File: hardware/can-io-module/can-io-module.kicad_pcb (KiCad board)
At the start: 2 copper layers, 96 x 86 mm, 12 parts, among them J1 ECU_FCI_24P_RightAngle, Q4 RELAY1 MOSFET, Q5 RELAY2 MOSFET, U1 STM32G0B1CBT6, U10 MAX31855K, U11 FLEX SCHMITT, U2 LMR16006Y-Q1, U5 74HCT4051-1K, U6 74HCT4051-4K7, U7 L9613, U8 TJA1051T/3, U9 TLV9002-Q1

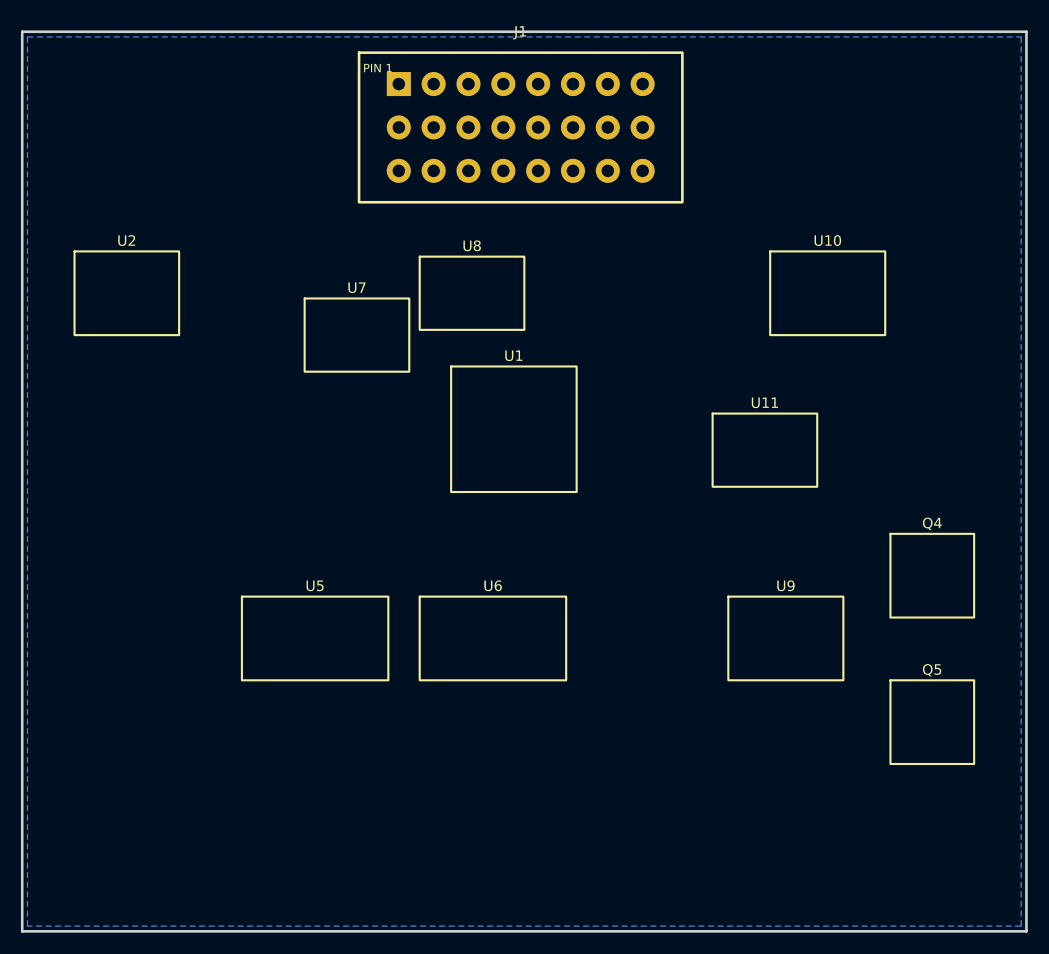
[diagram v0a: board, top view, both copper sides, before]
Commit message: feat: generate connected CAN IO revision B PCB
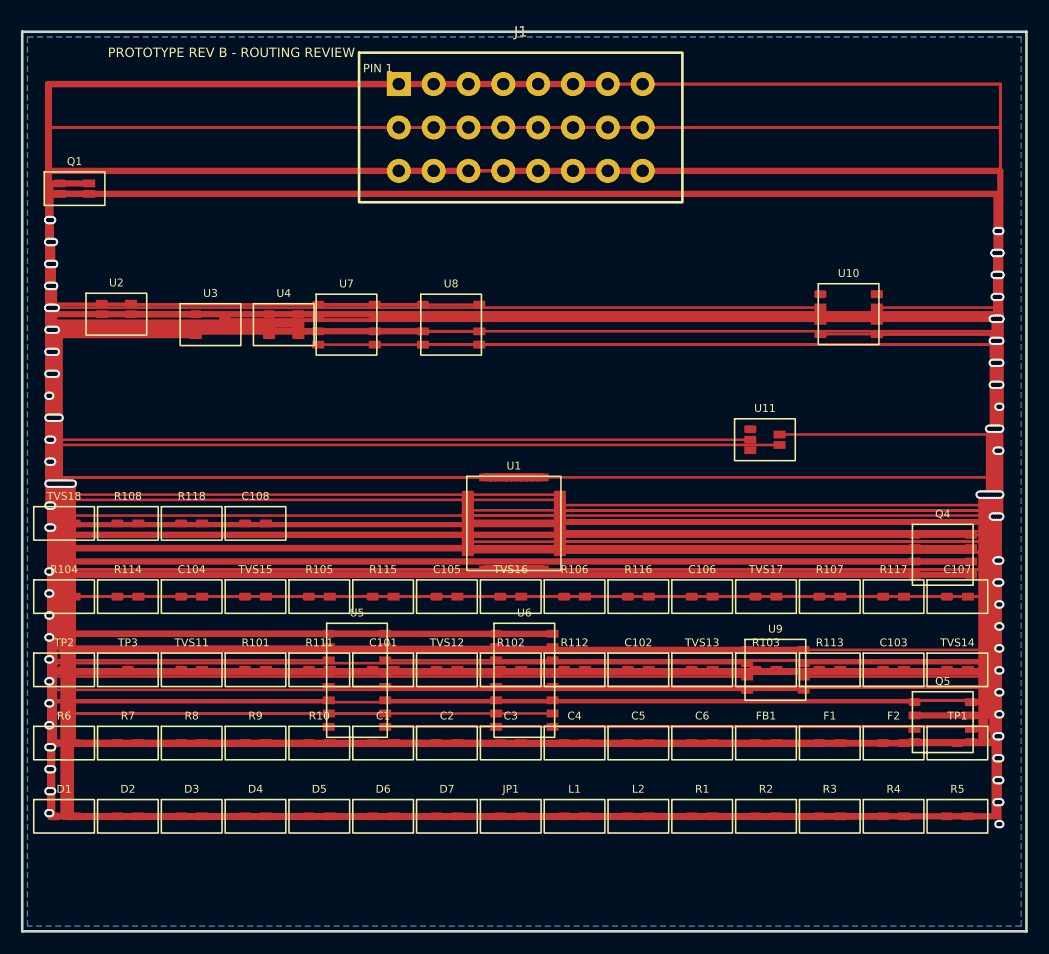
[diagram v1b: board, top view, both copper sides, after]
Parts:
- added C1: 10uF 50V input, DIY_DASH:1210, F.Cu at (54.5, 88.0)
- added C101: 100nF ADC filter, DIY_DASH:0603, F.Cu at (54.5, 81.0)
- added C102: 100nF ADC filter, DIY_DASH:0603, F.Cu at (78.9, 81.0)
- added C103: 100nF ADC filter, DIY_DASH:0603, F.Cu at (103.3, 81.0)
- added C104: 100nF ADC filter, DIY_DASH:0603, F.Cu at (36.2, 74.0)
- added C105: 100nF ADC filter, DIY_DASH:0603, F.Cu at (60.6, 74.0)
- added C106: 100nF ADC filter, DIY_DASH:0603, F.Cu at (85.0, 74.0)
- added C107: 100nF ADC filter, DIY_DASH:0603, F.Cu at (109.4, 74.0)
- added C108: 100nF ADC filter, DIY_DASH:0603, F.Cu at (42.3, 67.0)
- added C2: 22uF 10V buck output, DIY_DASH:1206, F.Cu at (60.6, 88.0)
- added C3: 4.7uF 10V 3V3 bulk, DIY_DASH:0805, F.Cu at (66.7, 88.0)
- added C4: 100nF U1 VDD1, DIY_DASH:0603, F.Cu at (72.8, 88.0)
- added C5: 100nF U1 VDD2, DIY_DASH:0603, F.Cu at (78.9, 88.0)
- added C6: 100nF U1 VDDA, DIY_DASH:0603, F.Cu at (85.0, 88.0)
- added D1: SMBJ33A, DIY_DASH:SMB_DO-214AA, F.Cu at (24.0, 95.0)
- added D2: Buck catch diode 60V, DIY_DASH:SMA_DO-214AC, F.Cu at (30.1, 95.0)
- added D3: CAN TVS, DIY_DASH:SOT23, F.Cu at (36.2, 95.0)
- added D4: K-line TVS 24V, DIY_DASH:SMA_DO-214AC, F.Cu at (42.3, 95.0)
- added D5: Flex TVS 5V, DIY_DASH:SOD323, F.Cu at (48.4, 95.0)
- added D6: AOUT1 ESD, DIY_DASH:SOD323, F.Cu at (54.5, 95.0)
- added D7: AOUT2 ESD, DIY_DASH:SOD323, F.Cu at (60.6, 95.0)
- added F1: 1A input fuse, DIY_DASH:NANO2_2410, F.Cu at (97.2, 88.0)
- added F2: 250mA resettable sensor fuse, DIY_DASH:1206, F.Cu at (103.3, 88.0)
- added FB1: 600R ferrite VDDA, DIY_DASH:0603, F.Cu at (91.1, 88.0)
- added JP1: 120R CAN termination, DIY_DASH:0603, F.Cu at (66.7, 95.0)
- added L1: 22uH buck inductor, DIY_DASH:5.5x5.5mm, F.Cu at (72.8, 95.0)
- added L2: CAN common-mode choke, DIY_DASH:1812_common-mode, F.Cu at (78.9, 95.0)
- added Q1: 60V P-channel reverse polarity, DIY_DASH:PowerPAK_SO-8, F.Cu at (25.0, 35.0)
- added R1: 1.00k 1% excitation, DIY_DASH:0603, F.Cu at (85.0, 95.0)
- added R10: 100k BOOT0 pull-down, DIY_DASH:0603, F.Cu at (48.4, 88.0)
- added R101: 10.0k 1% AIN series, DIY_DASH:0603, F.Cu at (42.3, 81.0)
- added R102: 10.0k 1% AIN series, DIY_DASH:0603, F.Cu at (66.7, 81.0)
- added R103: 10.0k 1% AIN series, DIY_DASH:0603, F.Cu at (91.1, 81.0)
- added R104: 10.0k 1% AIN series, DIY_DASH:0603, F.Cu at (24.0, 74.0)
- added R105: 10.0k 1% AIN series, DIY_DASH:0603, F.Cu at (48.4, 74.0)
- added R106: 10.0k 1% AIN series, DIY_DASH:0603, F.Cu at (72.8, 74.0)
- added R107: 10.0k 1% AIN series, DIY_DASH:0603, F.Cu at (97.2, 74.0)
- added R108: 10.0k 1% AIN series, DIY_DASH:0603, F.Cu at (30.1, 67.0)
- added R111: 15.0k 1% AIN lower, DIY_DASH:0603, F.Cu at (48.4, 81.0)
- added R112: 15.0k 1% AIN lower, DIY_DASH:0603, F.Cu at (72.8, 81.0)
- added R113: 15.0k 1% AIN lower, DIY_DASH:0603, F.Cu at (97.2, 81.0)
- added R114: 15.0k 1% AIN lower, DIY_DASH:0603, F.Cu at (30.1, 74.0)
- added R115: 15.0k 1% AIN lower, DIY_DASH:0603, F.Cu at (54.5, 74.0)
- added R116: 15.0k 1% AIN lower, DIY_DASH:0603, F.Cu at (78.9, 74.0)
- added R117: 15.0k 1% AIN lower, DIY_DASH:0603, F.Cu at (103.3, 74.0)
- added R118: 15.0k 1% AIN lower, DIY_DASH:0603, F.Cu at (36.2, 67.0)
- added R2: 4.70k 1% excitation, DIY_DASH:0603, F.Cu at (91.1, 95.0)
- added R3: 100k mux enable safe-state, DIY_DASH:0603, F.Cu at (97.2, 95.0)
- added R4: 100k mux enable safe-state, DIY_DASH:0603, F.Cu at (103.3, 95.0)
- added R5: 100k relay gate pull-down, DIY_DASH:0603, F.Cu at (109.4, 95.0)
- added R6: 100k relay gate pull-down, DIY_DASH:0603, F.Cu at (24.0, 88.0)
- added R7: 220R AOUT1 isolation, DIY_DASH:0603, F.Cu at (30.1, 88.0)
- added R8: 220R AOUT2 isolation, DIY_DASH:0603, F.Cu at (36.2, 88.0)
- added R9: 10k NRST pull-up, DIY_DASH:0603, F.Cu at (42.3, 88.0)
- added TP1: SWDIO, DIY_DASH:Test_pad, F.Cu at (109.4, 88.0)
- added TP2: SWCLK, DIY_DASH:Test_pad, F.Cu at (24.0, 81.0)
- added TP3: NRST, DIY_DASH:Test_pad, F.Cu at (30.1, 81.0)
- added TVS11: AIN1 low-leakage ESD, DIY_DASH:SOD323, F.Cu at (36.2, 81.0)
- added TVS12: AIN2 low-leakage ESD, DIY_DASH:SOD323, F.Cu at (60.6, 81.0)
- added TVS13: AIN3 low-leakage ESD, DIY_DASH:SOD323, F.Cu at (85.0, 81.0)
- added TVS14: AIN4 low-leakage ESD, DIY_DASH:SOD323, F.Cu at (109.4, 81.0)
- added TVS15: AIN5 low-leakage ESD, DIY_DASH:SOD323, F.Cu at (42.3, 74.0)
- added TVS16: AIN6 low-leakage ESD, DIY_DASH:SOD323, F.Cu at (66.7, 74.0)
- added TVS17: AIN7 low-leakage ESD, DIY_DASH:SOD323, F.Cu at (91.1, 74.0)
- added TVS18: AIN8 low-leakage ESD, DIY_DASH:SOD323, F.Cu at (24.0, 67.0)
- added U3: 3V3 LDO 300mA, DIY_DASH:SOT-23-5, F.Cu at (38.0, 48.0)
- added U4: SENSOR_5V load switch, DIY_DASH:SC70-6, F.Cu at (45.0, 48.0)
- Q4: value RELAY1 MOSFET -> 60V logic N-MOS RELAY1; footprint DIY_DASH:PLACEMENT_BLOCK -> DIY_DASH:LFPAK56
- Q5: value RELAY2 MOSFET -> 60V logic N-MOS RELAY2; footprint DIY_DASH:PLACEMENT_BLOCK -> DIY_DASH:LFPAK56
- U1: footprint DIY_DASH:PLACEMENT_BLOCK -> DIY_DASH:LQFP-48_7x7mm
- U10: value MAX31855K -> MAX31855KASA+; footprint DIY_DASH:PLACEMENT_BLOCK -> DIY_DASH:SOIC-8_narrow
- U11: value FLEX SCHMITT -> Schmitt Flex front end; footprint DIY_DASH:PLACEMENT_BLOCK -> DIY_DASH:SOT-353
- U2: footprint DIY_DASH:PLACEMENT_BLOCK -> DIY_DASH:SOT-23-THN-6_DDC
- U5: value 74HCT4051-1K -> 74HCT4051 1K excitation; footprint DIY_DASH:PLACEMENT_BLOCK -> DIY_DASH:SOIC-16
- U6: value 74HCT4051-4K7 -> 74HCT4051 4K7 excitation; footprint DIY_DASH:PLACEMENT_BLOCK -> DIY_DASH:SOIC-16
- U7: footprint DIY_DASH:PLACEMENT_BLOCK -> DIY_DASH:SO-8
- U8: footprint DIY_DASH:PLACEMENT_BLOCK -> DIY_DASH:SO-8_SOT96-1
- U9: footprint DIY_DASH:PLACEMENT_BLOCK -> DIY_DASH:SOIC-8
- moved U1 9.00 mm to (67.0, 67.0)
- moved U5 5.66 mm to (52.0, 82.0)
- moved U6 5.00 mm to (68.0, 82.0)
- moved U8 3.61 mm to (61.0, 48.0)
- moved U9 3.16 mm to (92.0, 81.0)
- moved U10 2.83 mm to (99.0, 47.0)
- moved Q4 2.24 mm to (108.0, 70.0)
- moved U2 2.24 mm to (29.0, 47.0)
- moved U7 1.41 mm to (51.0, 48.0)
- moved Q5 1.00 mm to (108.0, 86.0)
- moved U11 1.00 mm to (91.0, 59.0)
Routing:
- net +5V: track 0.00 -> 937.6 mm, vias 0 -> 14
- net +3V3: track 0.00 -> 746.8 mm, vias 0 -> 12
- net RELAY_OUT1: track 0.00 -> 662.0 mm, vias 0 -> 7
- net VBAT_PROTECTED: track 0.00 -> 502.8 mm, vias 0 -> 5
- net AIN8: track 0.00 -> 427.8 mm, vias 0 -> 5
- net ADC_IN4: track 0.00 -> 420.4 mm, vias 0 -> 4
- net ADC_IN3: track 0.00 -> 410.4 mm, vias 0 -> 4
- net AIN2: track 0.00 -> 408.1 mm, vias 0 -> 5
- net AIN3: track 0.00 -> 394.7 mm, vias 0 -> 5
- net ADC_IN7: track 0.00 -> 393.0 mm, vias 0 -> 4
- net AIN4: track 0.00 -> 387.2 mm, vias 0 -> 5
- net AIN7: track 0.00 -> 382.8 mm, vias 0 -> 5
- net AIN6: track 0.00 -> 371.9 mm, vias 0 -> 5
- net ADC_IN8: track 0.00 -> 362.2 mm, vias 0 -> 4
- net CAN_H: track 0.00 -> 353.5 mm, vias 0 -> 4
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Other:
- board text added: "PROTOTYPE REV B - ROUTING REVIEW"
- board text added: "ZONE_POWER ZONE_MCU_COMMS ZONE_ANALOG ZONE_EGT ZONE_OUTPUTS"
- board text removed: "ANALOG INPUTS"
- board text removed: "EGT - QUIET ZONE"
- board text removed: "MCU / CAN / K-LINE"
- board text removed: "OUTPUTS"
- board text removed: "POWER"
- board text removed: "PROTOTYPE REV A"
- board text removed: "ZONE_ANALOG"
- board text removed: "ZONE_EGT"
- board text removed: "ZONE_MCU_COMMS"
- board text removed: "ZONE_OUTPUTS"
- board text removed: "ZONE_POWER"

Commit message: fix: optimize two-layer CAN IO placement
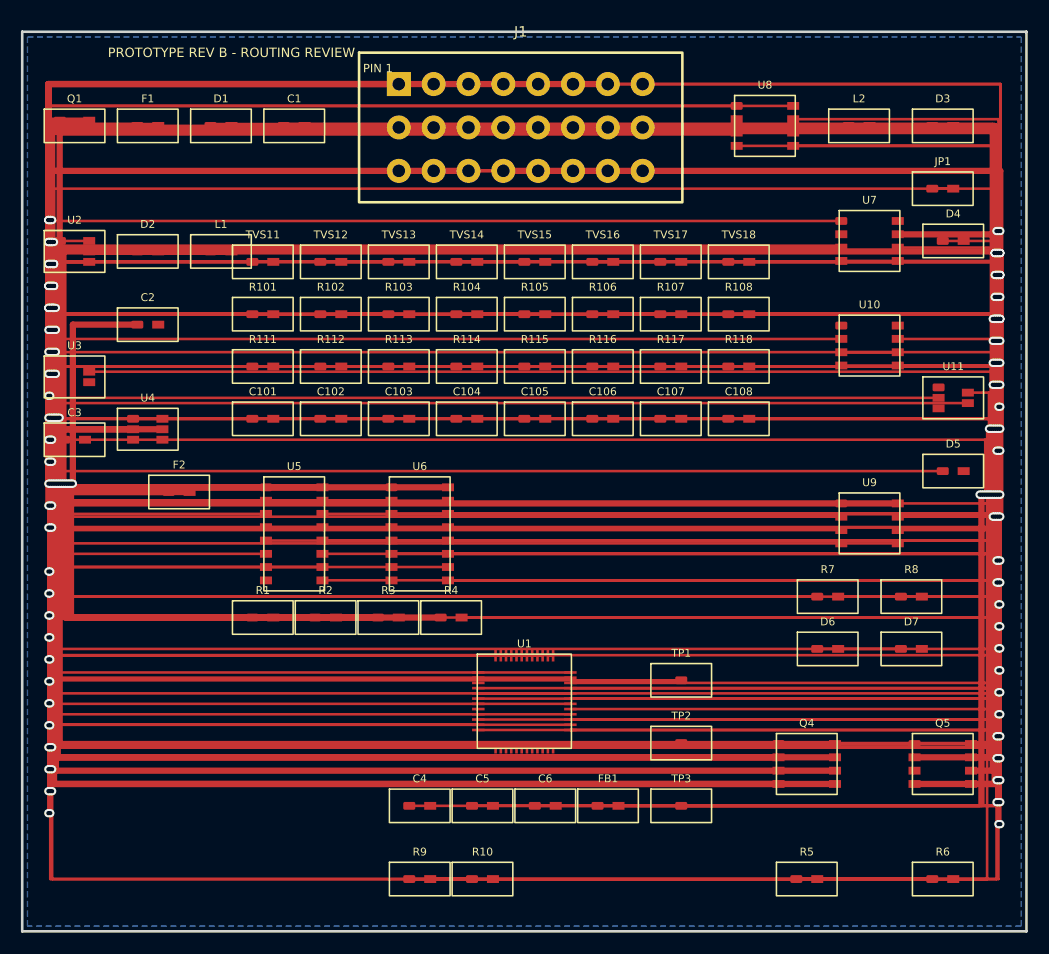
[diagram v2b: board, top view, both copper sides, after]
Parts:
- moved D3 97.5 mm to (108.0, 29.0)
- moved F1 87.9 mm to (32.0, 29.0)
- moved D4 86.5 mm to (109.0, 40.0)
- moved R6 85.0 mm to (108.0, 101.0)
- moved JP1 72.8 mm to (108.0, 35.0)
- moved F2 72.4 mm to (35.0, 64.0)
- moved R8 70.2 mm to (105.0, 74.0)
- moved L2 69.3 mm to (100.0, 29.0)
- moved TVS18 69.2 mm to (88.5, 42.0)
- moved D5 69.0 mm to (109.0, 62.0)
- moved R7 68.3 mm to (97.0, 74.0)
- moved D1 67.7 mm to (39.0, 29.0)
- moved L1 63.7 mm to (39.0, 41.0)
- moved R108 61.7 mm to (88.5, 47.0)
- moved TVS14 61.0 mm to (62.5, 42.0)
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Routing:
- net +5V: track 937.6 -> 610.4 mm
- net CAN_H: track 353.5 -> 127.5 mm
- net ADC_IN3: track 410.4 -> 217.8 mm
- net SENSOR_5V: track 349.4 -> 161.8 mm
- net ADC_IN8: track 362.2 -> 177.3 mm
- net K_LINE: track 248.2 -> 80.3 mm
- net AIN3: track 394.7 -> 229.6 mm
- net ADC_IN4: track 420.4 -> 273.1 mm
- net AIN8: track 427.8 -> 284.9 mm
- net AOUT1: track 272.9 -> 133.5 mm
- net AOUT2_OP: track 248.8 -> 120.0 mm
- net ADC_IN7: track 393.0 -> 281.1 mm
- net VBAT: track 170.2 -> 64.0 mm
- net AIN1: track 301.8 -> 201.1 mm
- net +3V3: track 746.8 -> 843.1 mm
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
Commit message: fix: preserve complete two-layer route
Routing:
- added copper zone on F.Cu, net POWER_GND
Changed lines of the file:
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@@
   (group "ROUTED_POWER_TREE" (id b7391667-93ed-535d-b822-70054c11cea7) (members))
   (group "ROUTED_COMMS_EGT_OUTPUTS" (id ce7aa9ae-598b-5771-b386-408a4e588b00) (members))
+  (zone (net 2) (net_name "POWER_GND") (layer "F.Cu") (hatch edge 0.5) (connect_pads (clearance 0.25)) (min_thickness 0.25) (fill yes (thermal_gap 0.3) (thermal_bridge_width 0.3)) (polygon (pts (xy 20.5 20.5) (xy 115.5 20.5) (xy 115.5 105.5) (xy 20.5 105.5))))
   (zone (net 2) (net_name "POWER_GND") (layer "B.Cu") (hatch edge 0.5) (connect_pads (clearance 0.25)) (min_thickness 0.25) (fill yes (thermal_gap 0.3) (thermal_bridge_width 0.3)) (polygon (pts (xy 20.5 20.5) (xy 115.5 20.5) (xy 115.5 105.5) (xy 20.5 105.5))))
   (gr_rect (start 20 20) (end 116 106) (stroke (width 0.25) (type default)) (fill none) (layer "Edge.Cuts"))
